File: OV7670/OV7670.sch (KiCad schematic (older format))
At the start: 7 parts, among them J1 OV7670, J2 PMOD1, J3 PMOD2, J4 PMOD1_EXT, J5 PMOD2_EXT, J6 EXT1, J7 EXT2

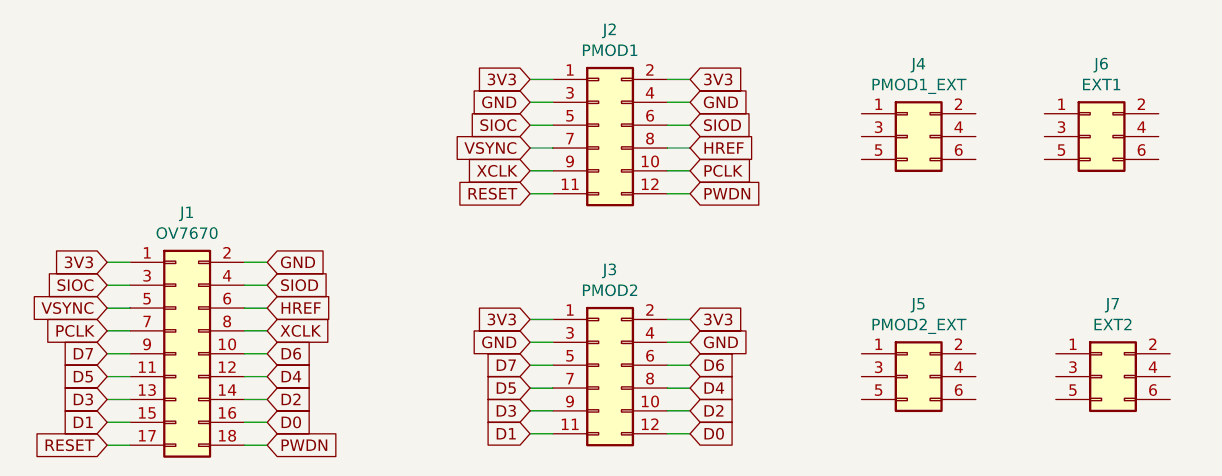
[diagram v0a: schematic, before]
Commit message: Routing OV7670 - files cleanup
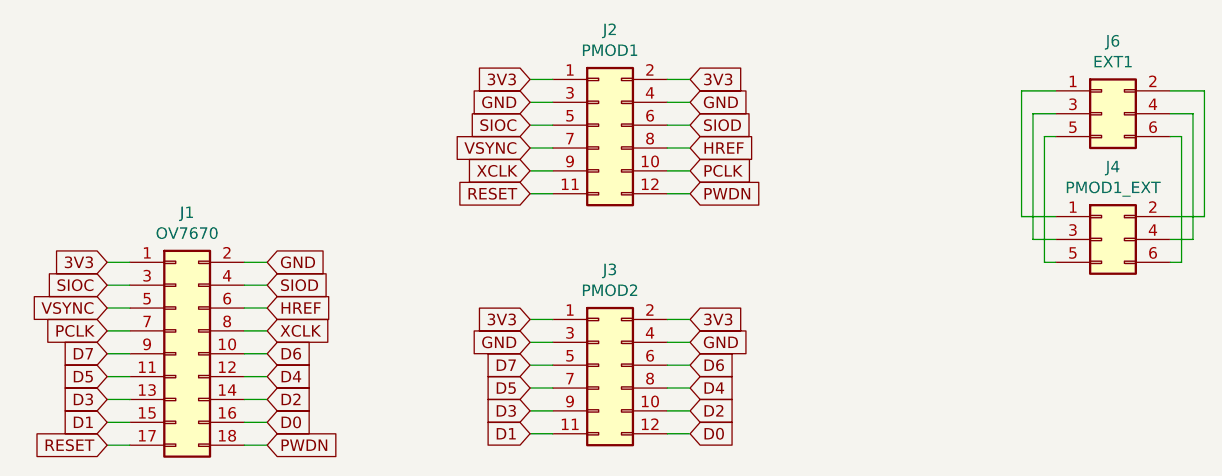
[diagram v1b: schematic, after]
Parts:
- removed J5: PMOD2_EXT, Connector_PinHeader_2.54mm:PinHeader_2x03_P2.54mm_Horizontal, symbol Connector_Generic:Conn_02x03_Odd_Even
- removed J7: EXT2, Connector_PinHeader_2.54mm:PinHeader_2x03_P2.54mm_Vertical, symbol Connector_Generic:Conn_02x03_Odd_Even
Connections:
- net at J4.1 (Pin_1): now also J6.1 (Pin_1)
- net at J4.2 (Pin_2): now also J6.2 (Pin_2)
- net at J4.3 (Pin_3): now also J6.3 (Pin_3)
- net at J4.4 (Pin_4): now also J6.4 (Pin_4)
- net at J4.5 (Pin_5): now also J6.5 (Pin_5)
- net at J4.6 (Pin_6): now also J6.6 (Pin_6)
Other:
- moved on the sheet: J4, J6
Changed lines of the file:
@@
 L Connector_Generic:Conn_02x03_Odd_Even J4
 U 1 1 5BFD989D
-P 8900 3300
-F 0 "J4" H 8950 3617 50  0000 C CNN
-F 1 "PMOD1_EXT" H 8950 3526 50  0000 C CNN
-F 2 "Connector_PinHeader_2.54mm:PinHeader_2x03_P2.54mm_Horizontal" H 8900 3300 50  0001 C CNN
-F 3 "~" H 8900 3300 50  0001 C CNN
-	1    8900 3300
-	1    0    0    -1
-$EndComp
-$Comp
-L Connector_Generic:Conn_02x03_Odd_Even J5
-U 1 1 5BFD99E9
-P 8900 4350
-F 0 "J5" H 8950 4667 50  0000 C CNN
-F 1 "PMOD2_EXT" H 8950 4576 50  0000 C CNN
-F 2 "Connector_PinHeader_2.54mm:PinHeader_2x03_P2.54mm_Horizontal" H 8900 4350 50  0001 C CNN
-F 3 "~" H 8900 4350 50  0001 C CNN
-	1    8900 4350
+P 9750 3750
+F 0 "J4" H 9800 4067 50  0000 C CNN
+F 1 "PMOD1_EXT" H 9800 3976 50  0000 C CNN
+F 2 "Connector_PinHeader_2.54mm:PinHeader_2x03_P2.54mm_Horizontal" H 9750 3750 50  0001 C CNN
+F 3 "~" H 9750 3750 50  0001 C CNN
+	1    9750 3750
 	1    0    0    -1
 $EndComp
@@
 L Connector_Generic:Conn_02x03_Odd_Even J6
 U 1 1 5BFD9AAC
-P 9700 3300
-F 0 "J6" H 9750 3617 50  0000 C CNN
-F 1 "EXT1" H 9750 3526 50  0000 C CNN
-F 2 "Connector_PinHeader_2.54mm:PinHeader_2x03_P2.54mm_Vertical" H 9700 3300 50  0001 C CNN
-F 3 "~" H 9700 3300 50  0001 C CNN
-	1    9700 3300
+P 9750 3200
+F 0 "J6" H 9800 3517 50  0000 C CNN
+F 1 "EXT1" H 9800 3426 50  0000 C CNN
+F 2 "Connector_PinHeader_2.54mm:PinHeader_2x03_P2.54mm_Vertical" H 9750 3200 50  0001 C CNN
+F 3 "~" H 9750 3200 50  0001 C CNN
+	1    9750 3200
 	1    0    0    -1
 $EndComp
-$Comp
-L Connector_Generic:Conn_02x03_Odd_Even J7
-U 1 1 5BFD9AE4
-P 9750 4350
-F 0 "J7" H 9800 4667 50  0000 C CNN
-F 1 "EXT2" H 9800 4576 50  0000 C CNN
-F 2 "Connector_PinHeader_2.54mm:PinHeader_2x03_P2.54mm_Vertical" H 9750 4350 50  0001 C CNN
-F 3 "~" H 9750 4350 50  0001 C CNN
-	1    9750 4350
-	1    0    0    -1
-$EndComp
+Wire Wire Line
+	9550 3200 9450 3200
+Wire Wire Line
+	9450 3200 9450 3750
+Wire Wire Line
+	9450 3750 9550 3750
+Wire Wire Line
+	9550 3300 9500 3300
+Wire Wire Line
+	9500 3300 9500 3850
+Wire Wire Line
+	9500 3850 9550 3850
+Wire Wire Line
+	10050 3850 10100 3850
+Wire Wire Line
+	10100 3850 10100 3300
+Wire Wire Line
+	10100 3300 10050 3300
+Wire Wire Line
+	10050 3200 10150 3200
+Wire Wire Line
+	10150 3200 10150 3750
+Wire Wire Line
+	10150 3750 10050 3750
+Wire Wire Line
+	10050 3650 10200 3650
+Wire Wire Line
+	10200 3650 10200 3100
+Wire Wire Line
+	10200 3100 10050 3100
+Wire Wire Line
+	9550 3100 9400 3100
+Wire Wire Line
+	9400 3100 9400 3650
+Wire Wire Line
+	9400 3650 9550 3650
 $EndSCHEMATC

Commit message: Adding GND and VCC to EXT connector
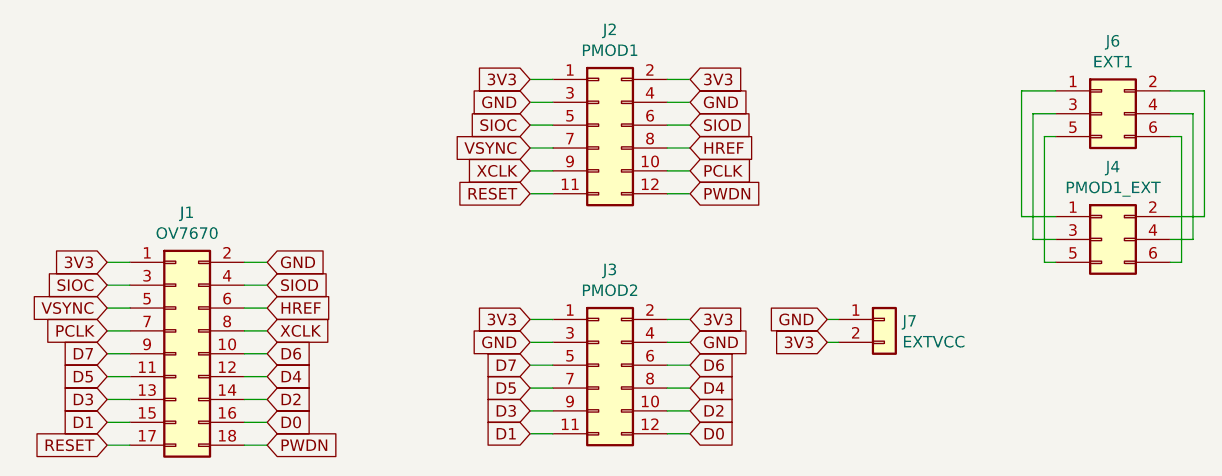
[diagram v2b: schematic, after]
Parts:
- added J7: EXTVCC, Connector_PinHeader_2.54mm:PinHeader_1x02_P2.54mm_Vertical, symbol Connector_Generic:Conn_01x02
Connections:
- net 3V3: now also J7.2 (Pin_2)
- net GND: now also J7.1 (Pin_1)
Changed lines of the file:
@@
 EESchema Schematic File Version 4
-LIBS:arduCam_RC522-cache
+LIBS:OV7670-cache
 EELAYER 26 0
 EELAYER END
@@
 Wire Wire Line
 	9400 3650 9550 3650
+$Comp
+L Connector_Generic:Conn_01x02 J7
+U 1 1 5BFF0749
+P 8800 4100
+F 0 "J7" H 8879 4092 50  0000 L CNN
+F 1 "EXTVCC" H 8879 4001 50  0000 L CNN
+F 2 "Connector_PinHeader_2.54mm:PinHeader_1x02_P2.54mm_Vertical" H 8800 4100 50  0001 C CNN
+F 3 "~" H 8800 4100 50  0001 C CNN
+	1    8800 4100
+	1    0    0    -1
+$EndComp
+Text GLabel 8550 4200 0    50   Input ~ 0
+3V3
+Text GLabel 8550 4100 0    50   Input ~ 0
+GND
+Wire Wire Line
+	8550 4100 8600 4100
+Wire Wire Line
+	8550 4200 8600 4200
 $EndSCHEMATC

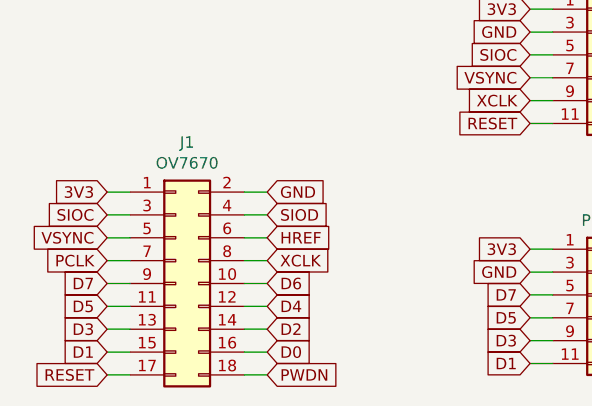
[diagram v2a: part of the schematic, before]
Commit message: Adding new OV7670 with gerber zip
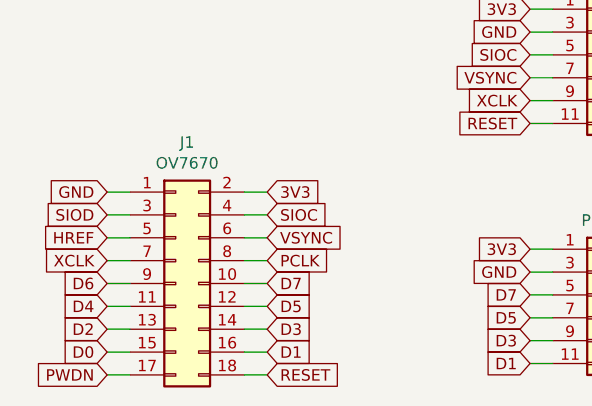
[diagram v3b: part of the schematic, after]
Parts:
- J1: footprint Connector_PinHeader_2.54mm:PinHeader_2x09_P2.54mm_Horizontal -> Connector_PinSocket_2.54mm:PinSocket_2x09_P2.54mm_Vertical
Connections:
- net 3V3: now also J1.2 (Pin_2); no longer J1.1 (Pin_1)
- net D0: now also J1.15 (Pin_15); no longer J1.16 (Pin_16)
- net D1: now also J1.16 (Pin_16); no longer J1.15 (Pin_15)
- net D2: now also J1.13 (Pin_13); no longer J1.14 (Pin_14)
- net D3: now also J1.14 (Pin_14); no longer J1.13 (Pin_13)
- net D4: now also J1.11 (Pin_11); no longer J1.12 (Pin_12)
- net D5: now also J1.12 (Pin_12); no longer J1.11 (Pin_11)
- net D6: now also J1.9 (Pin_9); no longer J1.10 (Pin_10)
- net D7: now also J1.10 (Pin_10); no longer J1.9 (Pin_9)
- net GND: now also J1.1 (Pin_1); no longer J1.2 (Pin_2)
- net HREF: now also J1.5 (Pin_5); no longer J1.6 (Pin_6)
- net PCLK: now also J1.8 (Pin_8); no longer J1.7 (Pin_7)
- net PWDN: now also J1.17 (Pin_17); no longer J1.18 (Pin_18)
- net RESET: now also J1.18 (Pin_18); no longer J1.17 (Pin_17)
- net SIOC: now also J1.4 (Pin_4); no longer J1.3 (Pin_3)
- net SIOD: now also J1.3 (Pin_3); no longer J1.4 (Pin_4)
- net VSYNC: now also J1.6 (Pin_6); no longer J1.5 (Pin_5)
- net XCLK: now also J1.7 (Pin_7); no longer J1.8 (Pin_8)
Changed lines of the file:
@@
 F 0 "J1" H 5750 4867 50  0000 C CNN
 F 1 "OV7670" H 5750 4776 50  0000 C CNN
-F 2 "Connector_PinHeader_2.54mm:PinHeader_2x09_P2.54mm_Horizontal" H 5700 4250 50  0001 C CNN
+F 2 "Connector_PinSocket_2.54mm:PinSocket_2x09_P2.54mm_Vertical" H 5700 4250 50  0001 C CNN
 F 3 "~" H 5700 4250 50  0001 C CNN
 	1    5700 4250
 	1    0    0    -1
 $EndComp
+Text GLabel 6100 3850 2    50   Input ~ 0
+3V3
+Text GLabel 6100 3950 2    50   Input ~ 0
+SIOC
+Text GLabel 6100 4150 2    50   Input ~ 0
+PCLK
+Text GLabel 6100 4250 2    50   Input ~ 0
+D7
+Text GLabel 6100 4350 2    50   Input ~ 0
+D5
+Text GLabel 6100 4450 2    50   Input ~ 0
+D3
+Text GLabel 6100 4550 2    50   Input ~ 0
+D1
+Text GLabel 6100 4650 2    50   Input ~ 0
+RESET
+Text GLabel 6100 4050 2    50   Input ~ 0
+VSYNC
 Text GLabel 5400 3850 0    50   Input ~ 0
-3V3
+GND
 Text GLabel 5400 3950 0    50   Input ~ 0
-SIOC
+SIOD
+Text GLabel 5400 4050 0    50   Input ~ 0
+HREF
 Text GLabel 5400 4150 0    50   Input ~ 0
-PCLK
+XCLK
 Text GLabel 5400 4250 0    50   Input ~ 0
-D7
+D6
 Text GLabel 5400 4350 0    50   Input ~ 0
-D5
+D4
 Text GLabel 5400 4450 0    50   Input ~ 0
-D3
+D2
 Text GLabel 5400 4550 0    50   Input ~ 0
-D1
+D0
 Text GLabel 5400 4650 0    50   Input ~ 0
-RESET
-Text GLabel 5400 4050 0    50   Input ~ 0
-VSYNC
-Text GLabel 6100 3850 2    50   Input ~ 0
-GND
-Text GLabel 6100 3950 2    50   Input ~ 0
-SIOD
-Text GLabel 6100 4050 2    50   Input ~ 0
-HREF
-Text GLabel 6100 4150 2    50   Input ~ 0
-XCLK
-Text GLabel 6100 4250 2    50   Input ~ 0
-D6
-Text GLabel 6100 4350 2    50   Input ~ 0
-D4
-Text GLabel 6100 4450 2    50   Input ~ 0
-D2
-Text GLabel 6100 4550 2    50   Input ~ 0
-D0
-Text GLabel 6100 4650 2    50   Input ~ 0
 PWDN
 Wire Wire Line
